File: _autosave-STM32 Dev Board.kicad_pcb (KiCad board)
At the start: 2 copper layers, 38.5 x 32.7 mm, 36 parts, among them J5 2 Pin JST, J6 USB_B_Micro, Q1 PMOS, U1 MCP2221AxML, U2 STM32F070F6Px, U3 MCP1824S, U4 MCP73113

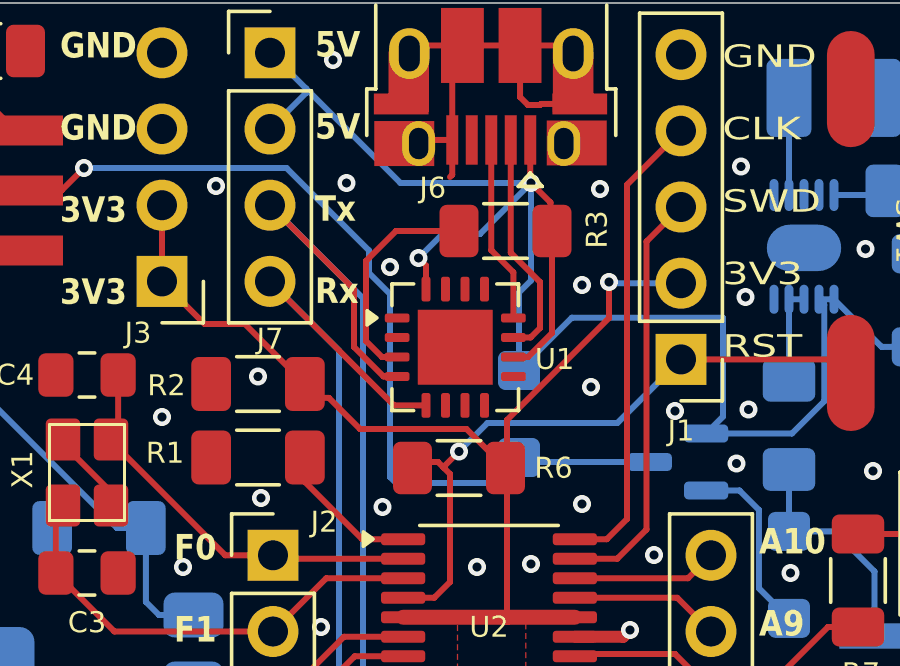
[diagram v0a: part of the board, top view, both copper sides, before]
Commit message: added ground via for UART-USB, updated gerber and drill files
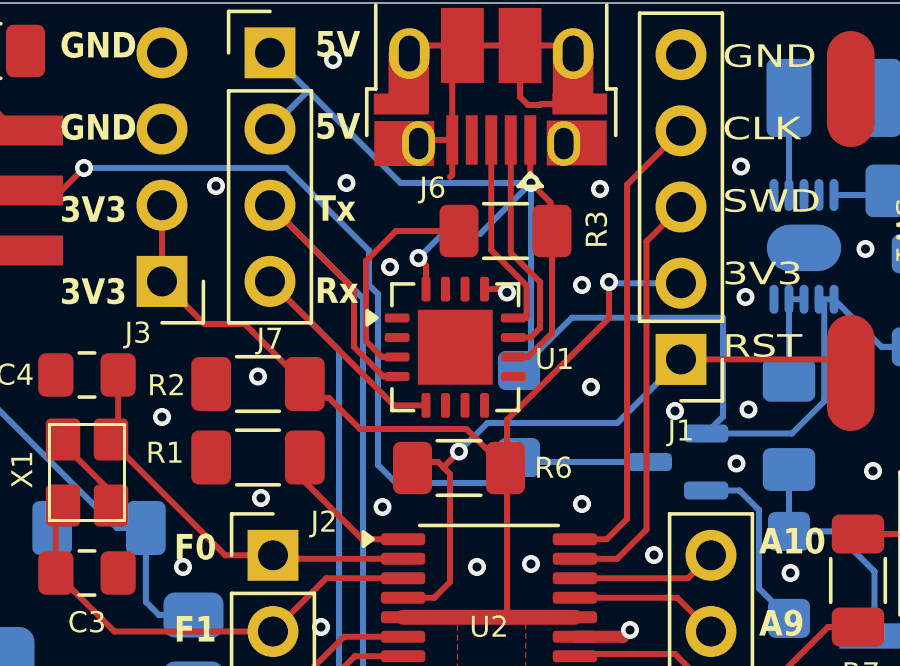
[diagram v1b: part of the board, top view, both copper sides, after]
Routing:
- net GND: track 20.0 -> 20.8 mm, vias 47 -> 48
- net Net-(J6-D+): track 6.24 -> 6.86 mm
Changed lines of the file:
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@@
 		(tenting front back)
 		(pcbplotparams
-			(layerselection 0x00000000_00000000_55555555_575555ff)
+			(layerselection 0x00000000_00000000_5555555f_ff55ffff)
 			(plot_on_all_layers_selection 0x00000000_00000000_00000000_00000000)
 			(disableapertmacros no)
@@
 	)
 	(segment
+		(start 141.15 75.5375)
+		(end 141.7875 75.5375)
+		(width 0.2)
+		(layer "F.Cu")
+		(net 2)
+	)
+	(segment
 		(start 140.415 67.415)
 		(end 140.075 67.755)
@@
 	)
 	(segment
+		(start 141.7875 75.5375)
+		(end 141.9 75.65)
+		(width 0.2)
+		(layer "F.Cu")
+		(net 2)
+	)
+	(segment
 		(start 140.415 67.415)
 		(end 138.915 67.415)
@@
 	)
 	(via
+		(at 141.9 75.65)
+		(size 0.6)
+		(drill 0.3)
+		(layers "F.Cu" "B.Cu")
+		(free yes)
+		(net 2)
+	)
+	(via
 		(at 155.5 95.5)
 		(size 5)
@@
 	)
 	(segment
-		(start 152.476 76.051)
-		(end 152.476 79.27266)
+		(start 142.7 77.85)
+		(end 142.3 78.25)
 		(width 0.2)
 		(layer "B.Cu")
@@
 	)
 	(segment
-		(start 148.5375 80.35)
-		(end 149.1 79.7875)
+		(start 152.476 76.051)
+		(end 152.476 79.27266)
 		(width 0.2)
 		(layer "B.Cu")
@@
 	)
 	(segment
-		(start 142.3 75.65)
-		(end 142.3 78.25)
+		(start 148.5375 80.35)
+		(end 149.1 79.7875)
 		(width 0.2)
 		(layer "B.Cu")
@@
 	)
 	(segment
+		(start 142.7 72)
+		(end 142.7 77.85)
+		(width 0.2)
+		(layer "B.Cu")
+		(net 19)
+	)
+	(segment
 		(start 149.1 79.7875)
 		(end 149.1 76.5)
@@
 	)
 	(segment
-		(start 142.7 72)
-		(end 142.7 75.25)
-		(width 0.2)
-		(layer "B.Cu")
-		(net 19)
-	)
-	(segment
 		(start 142.3 78.25)
 		(end 144.059 76.491)
@@
 	)
 	(segment
-		(start 142.7 75.25)
-		(end 142.3 75.65)
-		(width 0.2)
-		(layer "B.Cu")
-		(net 19)
-	)
-	(segment
 		(start 155.6 74.3625)
 		(end 155.6 70.4625)
@@
 	)
 	(segment
-		(start 142.1125 74.978186)
-		(end 141.375 74.240686)
+		(start 142.55 76.5)
+		(end 142.55 75.415686)
 		(width 0.2)
 		(layer "F.Cu")
@@
 	)
 	(segment
-		(start 142.1125 76.5)
-		(end 142.1125 74.978186)
+		(start 141.375 74.240686)
+		(end 141.375 70.565)
 		(width 0.2)
 		(layer "F.Cu")
@@
 	)
 	(segment
-		(start 141.375 74.240686)
-		(end 141.375 70.565)
+		(start 142.55 75.415686)
+		(end 141.375 74.240686)
+		(width 0.2)
+		(layer "F.Cu")
+		(net 27)
+	)
+	(segment
+		(start 142.1125 76.5)
+		(end 142.55 76.5)
 		(width 0.2)
 		(layer "F.Cu")
@@
 	)
 	(segment
-		(start 138 75.7)
-		(end 137.3 75)
+		(start 146.6625 81.3)
+		(end 142.45 81.3)
 		(width 0.2)
 		(layer "B.Cu")
@@
 	)
 	(segment
-		(start 146.6625 81.3)
-		(end 142.45 81.3)
+		(start 137.6 75.7)
+		(end 137.3 75.4)
 		(width 0.2)
 		(layer "B.Cu")
@@
 	)
 	(segment
-		(start 142.45 81.3)
-		(end 142.3 81.15)
+		(start 137.6 81.4)
+		(end 137.6 75.7)
 		(width 0.2)
 		(layer "B.Cu")
@@
 	)
 	(segment
-		(start 141.45 82)
-		(end 138.2 82)
+		(start 142.45 81.3)
+		(end 142.3 81.15)
 		(width 0.2)
 		(layer "B.Cu")
@@
 	)
 	(segment
-		(start 138 81.8)
-		(end 138 75.7)
+		(start 137.3 75.4)
+		(end 137.3 74.25)
 		(width 0.2)
 		(layer "B.Cu")
@@
 	)
 	(segment
-		(start 138.2 82)
-		(end 138 81.8)
+		(start 137.3 74.25)
+		(end 134.55 71.5)
 		(width 0.2)
 		(layer "B.Cu")
@@
 	)
 	(segment
-		(start 137.3 75)
-		(end 137.3 74.25)
+		(start 142.3 81.15)
+		(end 141.45 82)
 		(width 0.2)
 		(layer "B.Cu")
@@
 	)
 	(segment
-		(start 142.3 81.15)
-		(end 141.45 82)
+		(start 141.45 82)
+		(end 138.2 82)
 		(width 0.2)
 		(layer "B.Cu")
@@
 	)
 	(segment
-		(start 137.3 74.25)
-		(end 134.55 71.5)
+		(start 138.2 82)
+		(end 137.6 81.4)
 		(width 0.2)
 		(layer "B.Cu")
